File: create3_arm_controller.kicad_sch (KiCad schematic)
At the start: 4 parts

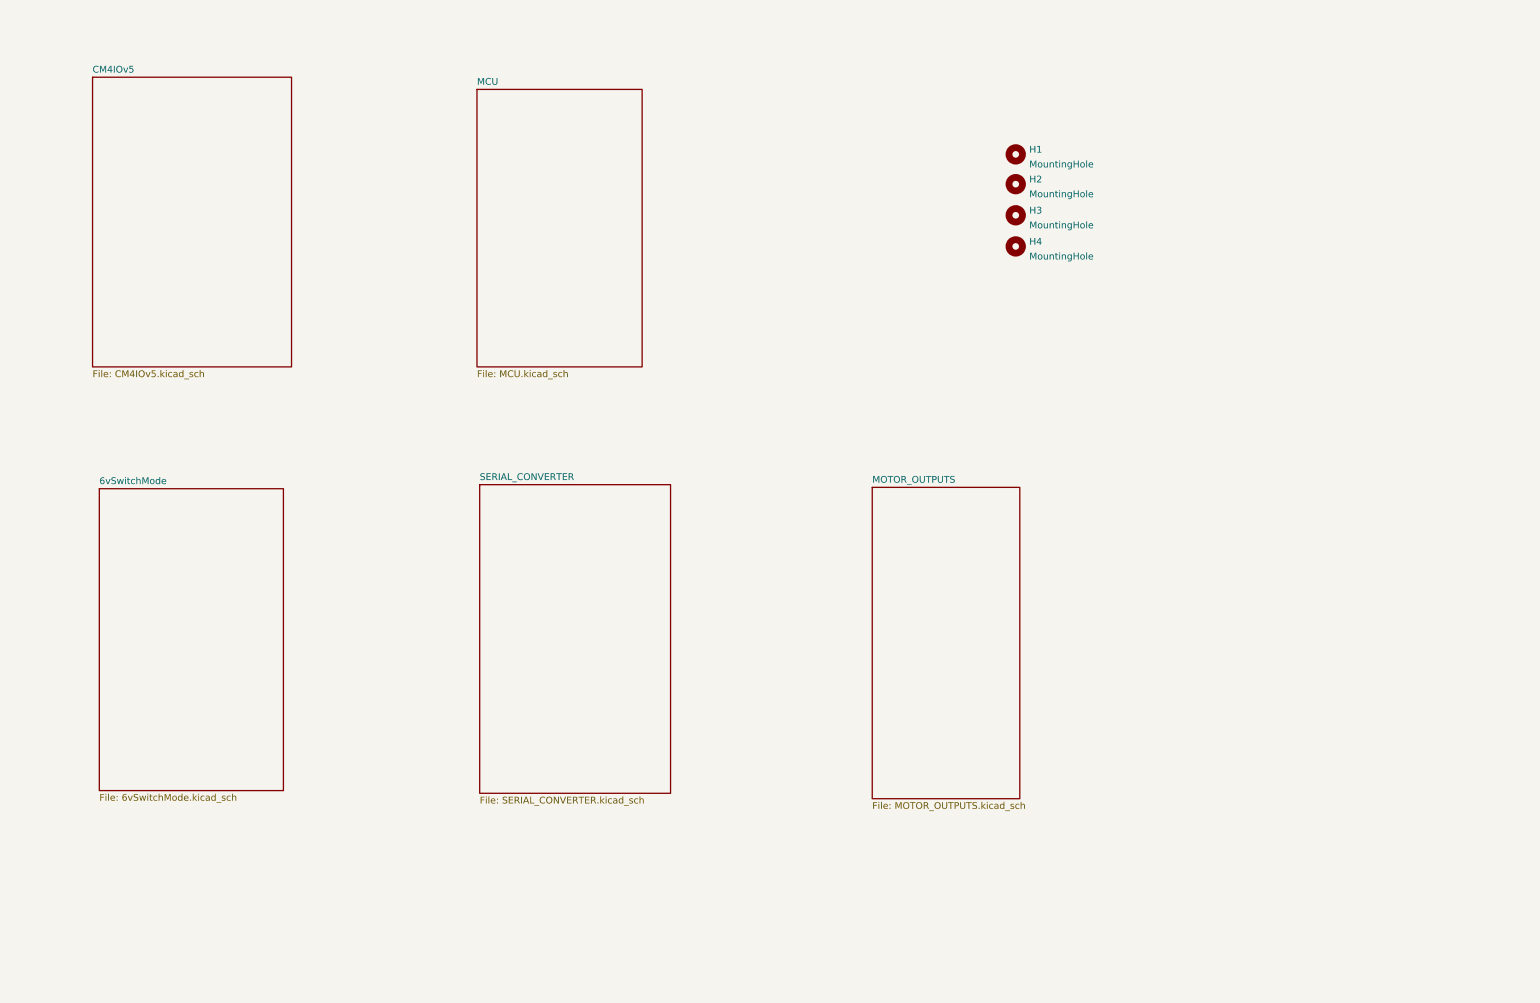
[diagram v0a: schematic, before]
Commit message: Initial layout and all parts added. Some pins still not connected to power
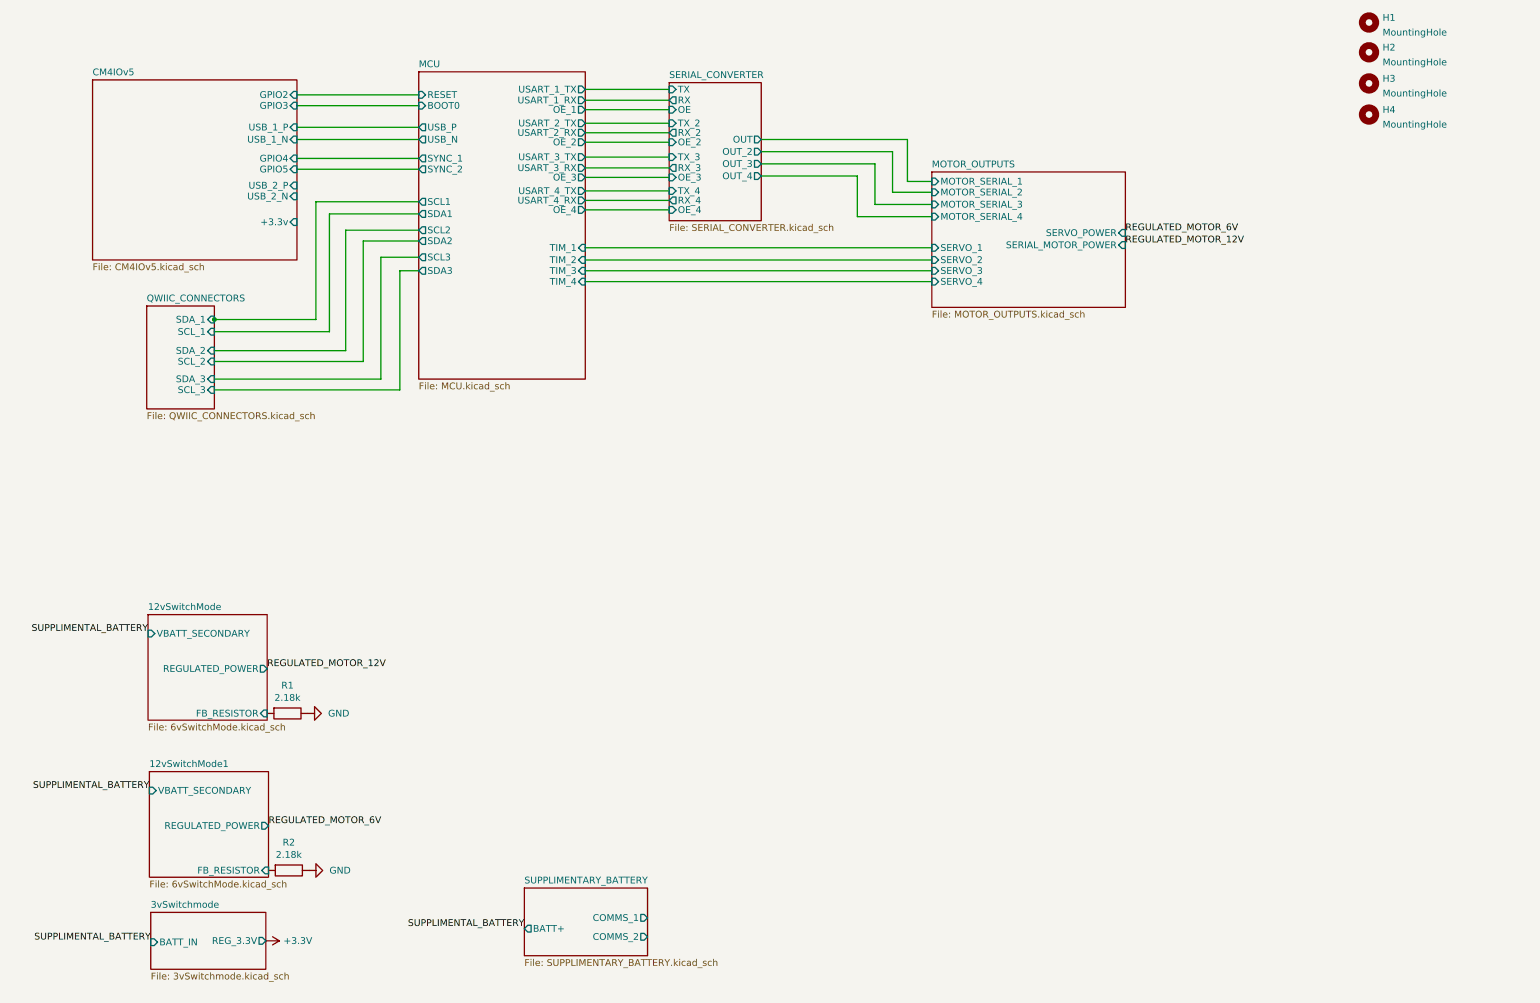
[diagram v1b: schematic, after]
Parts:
- added R1, R2: 2.18k, Resistor_SMD:R_0402_1005Metric, symbol Device:R
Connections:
- new net 12vSwitchMode/FB_RESISTOR: R1.2
- new net 12vSwitchMode1/FB_RESISTOR: R2.2
- new net GND: R1.1, R2.1
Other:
- sheet 6vSwitchMode renamed 12vSwitchMode
- added sheet 12vSwitchMode1 (6vSwitchMode.kicad_sch)
- added sheet 3vSwitchmode (3vSwitchmode.kicad_sch)
- added sheet QWIIC_CONNECTORS (QWIIC_CONNECTORS.kicad_sch)
- added sheet SUPPLIMENTARY_BATTERY (SUPPLIMENTARY_BATTERY.kicad_sch)
- sheet 12vSwitchMode ports: added FB_RESISTOR, REGULATED_POWER, VBATT_SECONDARY; removed none
- sheet CM4IOv5 ports: added +3.3v, GPIO2, GPIO3, GPIO4, GPIO5, USB_1_N, USB_1_P, USB_2_N, USB_2_P; removed none
- sheet MCU ports: added BOOT0, OE_1, OE_2, OE_3, OE_4, RESET, SCL1, SCL2, SCL3, SDA1, SDA2, SDA3, SYNC_1, SYNC_2, TIM_1, TIM_2, TIM_3, TIM_4, USART_1_RX, USART_1_TX, USART_2_RX, USART_2_TX, USART_3_RX, USART_3_TX, USART_4_RX, USART_4_TX, USB_N, USB_P; removed none
- sheet MOTOR_OUTPUTS ports: added MOTOR_SERIAL_1, MOTOR_SERIAL_2, MOTOR_SERIAL_3, MOTOR_SERIAL_4, SERIAL_MOTOR_POWER, SERVO_1, SERVO_2, SERVO_3, SERVO_4, SERVO_POWER; removed none
- sheet SERIAL_CONVERTER ports: added OE, OE_2, OE_3, OE_4, OUT, OUT_2, OUT_3, OUT_4, RX, RX_2, RX_3, RX_4, TX, TX_2, TX_3, TX_4; removed none
- moved on the sheet: H1, H2, H3, H4

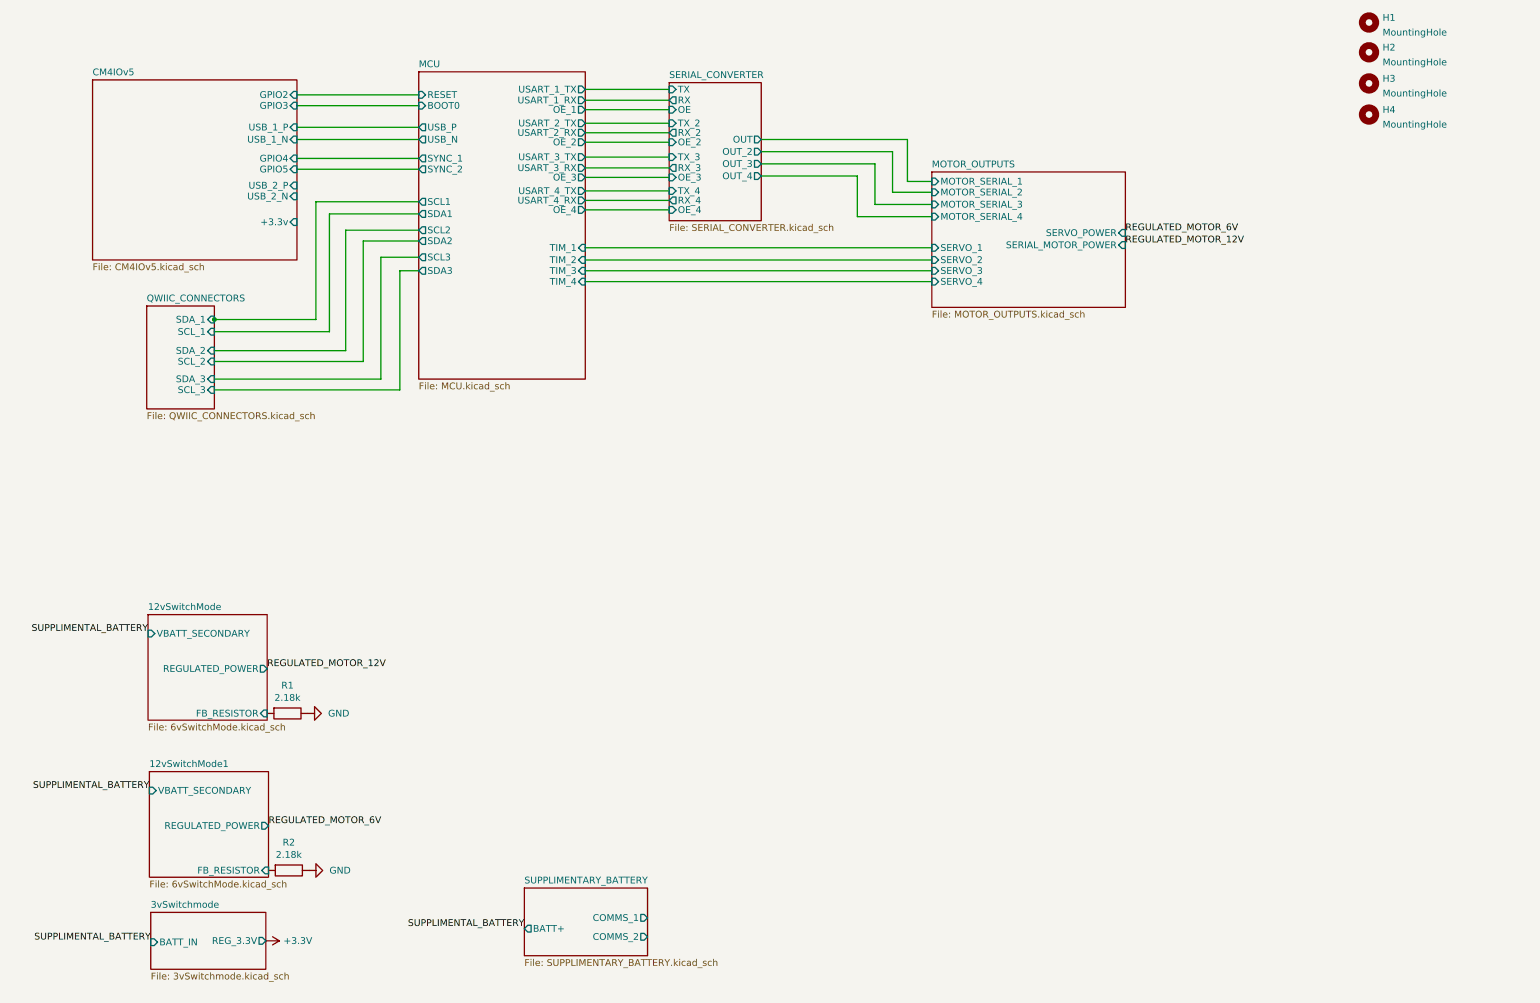
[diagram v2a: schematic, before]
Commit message: Added usb to ethernet and changed mcu to stm32g4
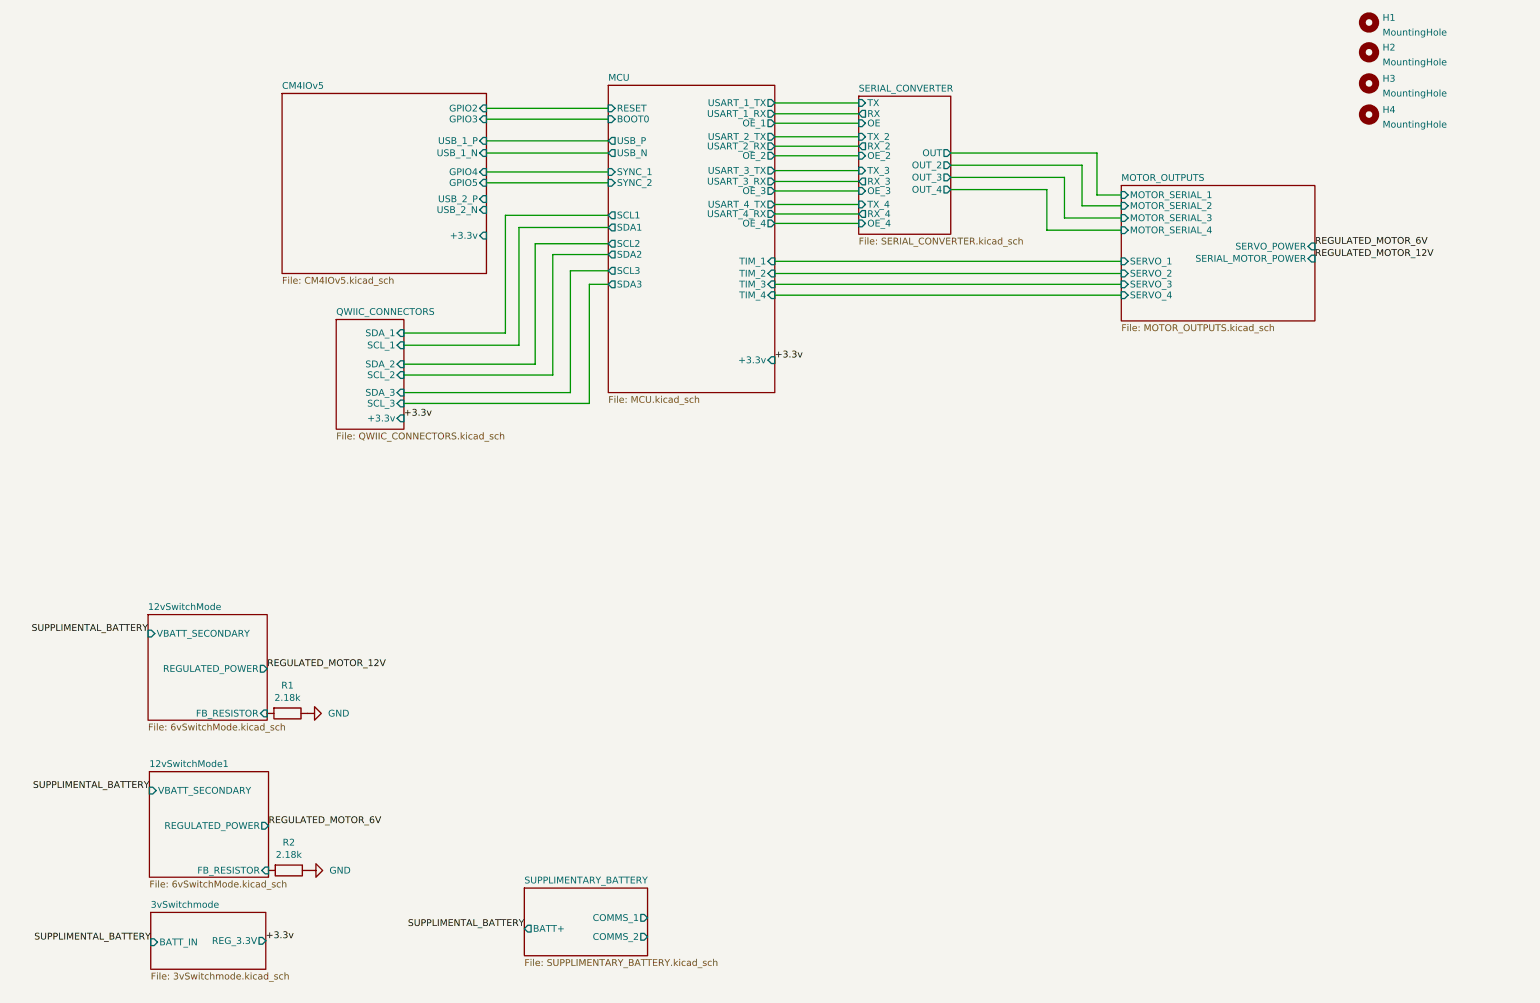
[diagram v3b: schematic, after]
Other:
- sheet MCU ports: added +3.3v; removed none
- sheet QWIIC_CONNECTORS ports: added +3.3v; removed none

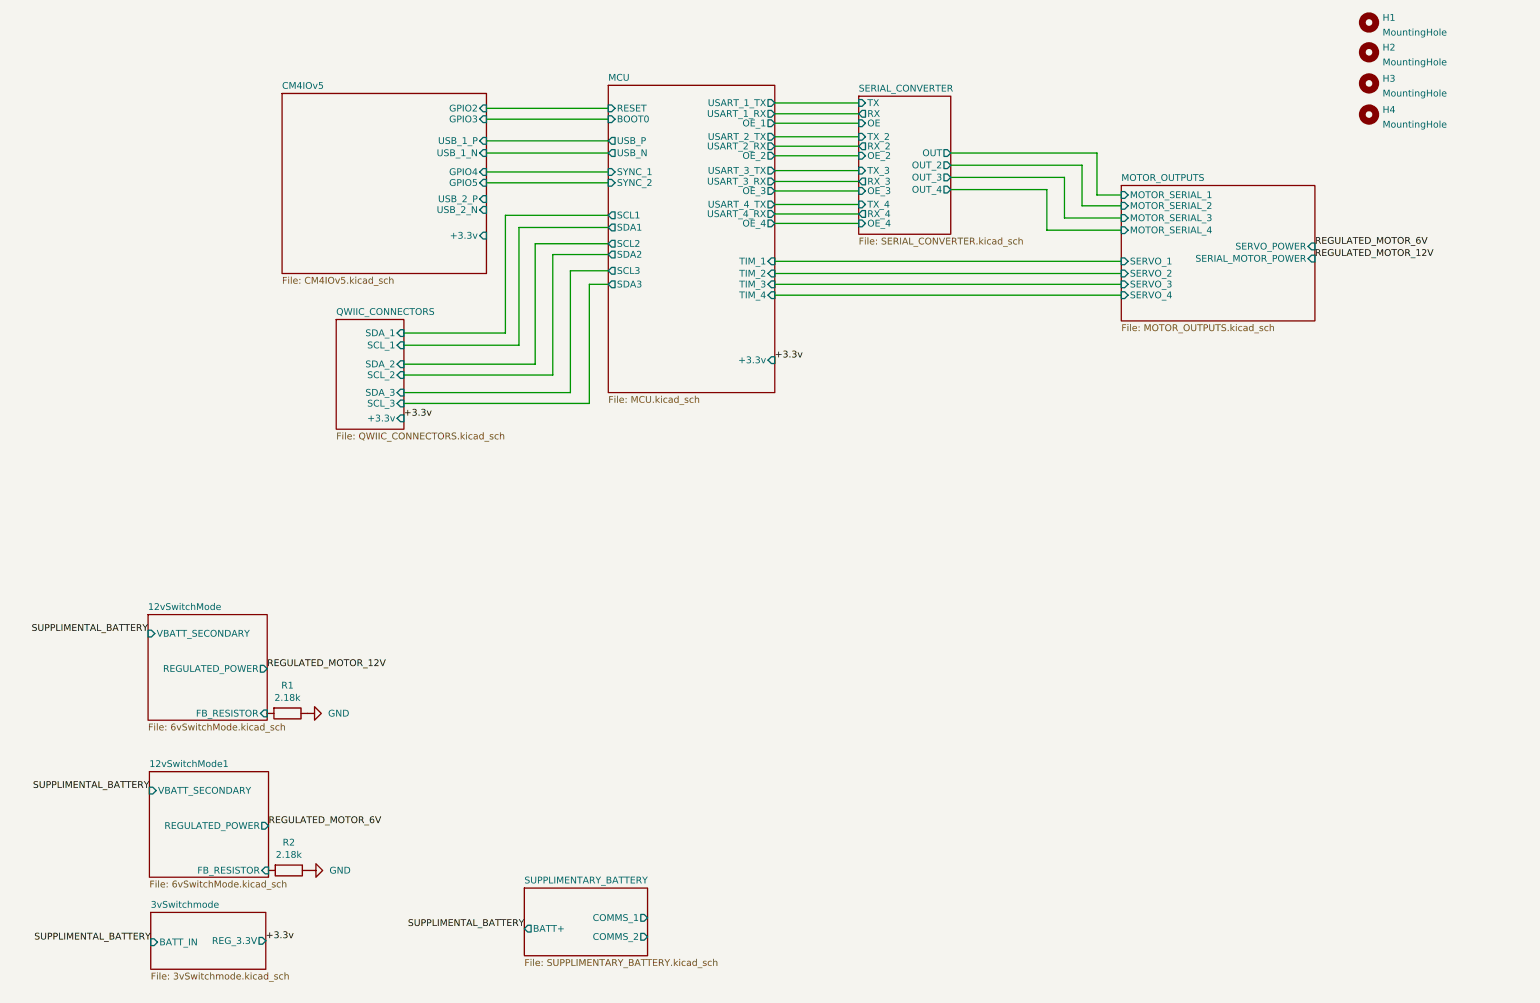
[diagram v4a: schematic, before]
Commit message: labeling and schematic cleanup
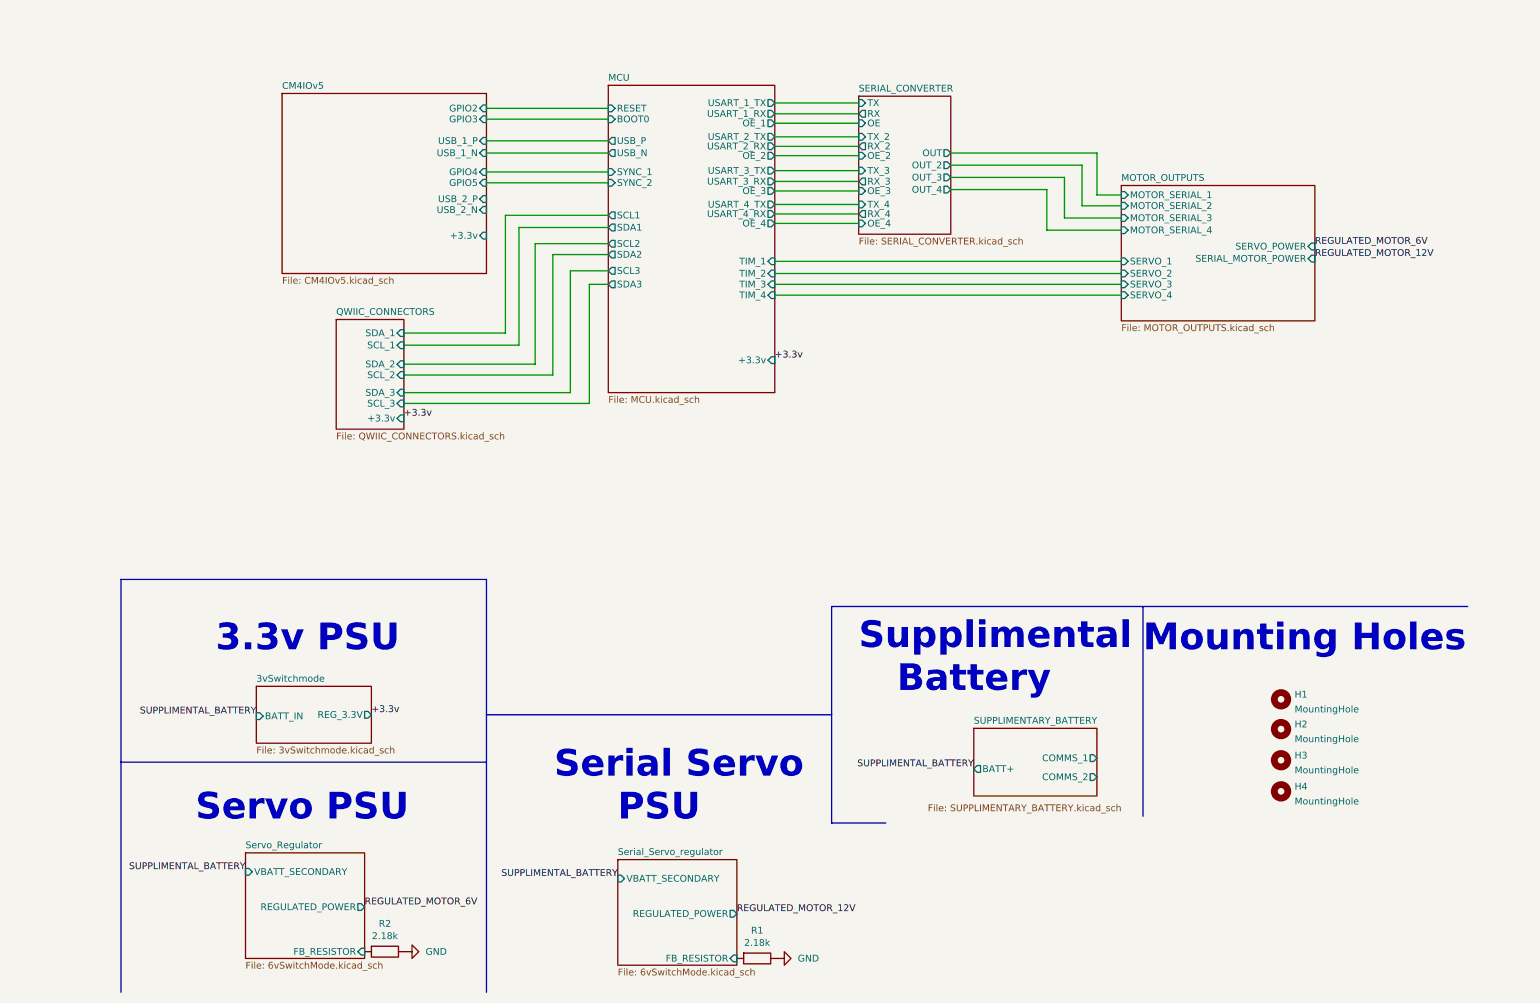
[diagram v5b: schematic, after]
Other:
- sheet 12vSwitchMode renamed Serial_Servo_regulator
- sheet 12vSwitchMode1 renamed Servo_Regulator
- note added: "3.3v PSU"
- note added: "Mounting Holes"
- note added: "Serial Servo PSU"
- note added: "Servo PSU"
- note added: "Supplimental Battery"
- moved on the sheet: H1, H2, H3, H4, R1, R2
